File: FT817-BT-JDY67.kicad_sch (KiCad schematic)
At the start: 35 parts, among them J1009 Mini-DIN-8PR, J1010 Mini-DIN-6PR, Q1 2N7002, Q2 TP0610, U1 JDY-67 Bluetooth Module, U2 LM1117MP-5.0

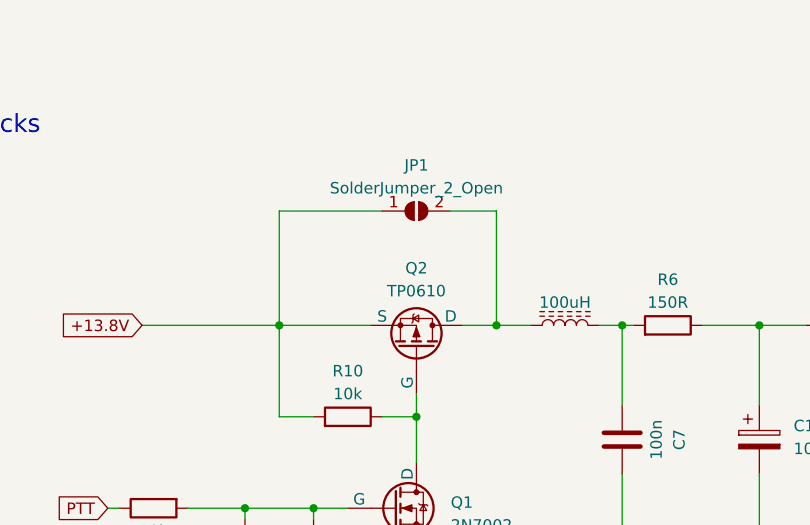
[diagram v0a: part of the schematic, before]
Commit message: Remove VCC control bypass jumper
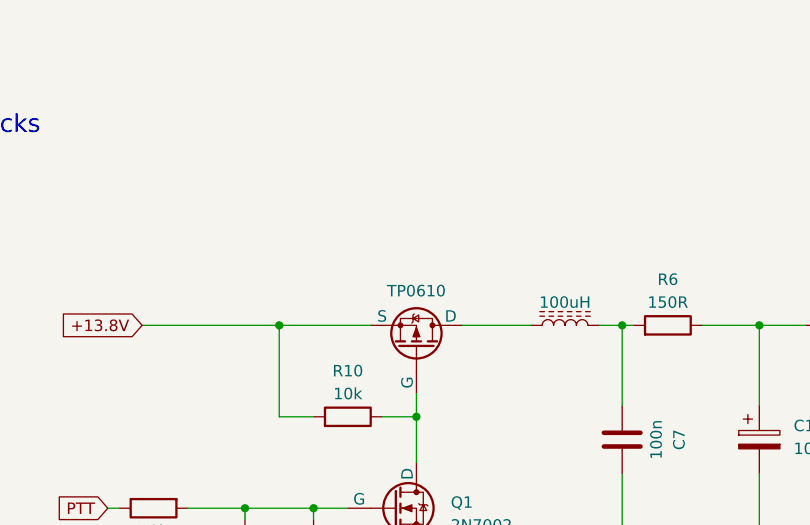
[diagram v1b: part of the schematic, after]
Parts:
- removed JP1: SolderJumper_2_Open, Jumper:SolderJumper-2_P1.3mm_Open_RoundedPad1.0x1.5mm, symbol Jumper:SolderJumper_2_Open
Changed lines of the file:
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@@
   (junction (at 204.47 144.78) (diameter 0) (color 0 0 0 0)
   )
-  (junction (at 171.45 50.8) (diameter 0) (color 0 0 0 0)
-  )
   (junction (at 147.32 50.8) (diameter 0) (color 0 0 0 0)
   )
@@
     (stroke (width 0) (type default))
   )
-  (wire (pts (xy 147.32 38.1) (xy 147.32 50.8))
-    (stroke (width 0) (type default))
-  )
   (wire (pts (xy 186.69 124.46) (xy 186.69 121.92))
     (stroke (width 0) (type default))
@@
     (stroke (width 0) (type default))
   )
-  (wire (pts (xy 167.64 50.8) (xy 171.45 50.8))
+  (wire (pts (xy 167.64 50.8) (xy 175.26 50.8))
     (stroke (width 0) (type default))
   )
@@
     (stroke (width 0) (type default))
   )
-  (wire (pts (xy 166.37 38.1) (xy 171.45 38.1))
-    (stroke (width 0) (type default))
-  )
   (wire (pts (xy 204.47 144.78) (xy 204.47 149.86))
     (stroke (width 0) (type default))
@@
     (stroke (width 0) (type default))
   )
-  (wire (pts (xy 171.45 38.1) (xy 171.45 50.8))
-    (stroke (width 0) (type default))
-  )
   (wire (pts (xy 137.16 71.12) (xy 143.51 71.12))
     (stroke (width 0) (type default))
@@
     (stroke (width 0) (type default))
   )
-  (wire (pts (xy 171.45 50.8) (xy 175.26 50.8))
-    (stroke (width 0) (type default))
-  )
   (wire (pts (xy 146.05 142.24) (xy 146.05 147.32))
-    (stroke (width 0) (type default))
-  )
-  (wire (pts (xy 158.75 38.1) (xy 147.32 38.1))
     (stroke (width 0) (type default))
   )
@@
     (in_bom yes) (on_board yes) (dnp no)
     (property "Reference" "Q2" (at 162.56 44.45 90)
-      (effects (font (size 1.27 1.27)))
+      (effects (font (size 1.27 1.27)) hide)
     )
     (property "Value" "TP0610" (at 162.56 46.99 90)
@@
         )
       )
-    )
-  )
-  (symbol (lib_id "Jumper:SolderJumper_2_Open") (at 162.56 38.1 0) (unit 1)
-    (in_bom yes) (on_board yes) (dnp no) (fields_autoplaced)
-    (property "Reference" "JP1" (at 162.56 33.02 0)
-      (effects (font (size 1.27 1.27)))
-    )
-    (property "Value" "SolderJumper_2_Open" (at 162.56 35.56 0)
-      (effects (font (size 1.27 1.27)))
-    )
-    (property "Footprint" "Jumper:SolderJumper-2_P1.3mm_Open_RoundedPad1.0x1.5mm" (at 162.56 38.1 0)
-      (effects (font (size 1.27 1.27)) hide)
-    )
-    (property "Datasheet" "~" (at 162.56 38.1 0)
-      (effects (font (size 1.27 1.27)) hide)
-    )
-    (pin "1")
-    (pin "2")
-    (instances
-      (project "FT817-BT-JDY67"
-        (path "/cfc49cd5-e50c-4df9-89f0-cc0db7d3dd1c"
-          (reference "JP1") (unit 1)
-        )
-      )

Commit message: update
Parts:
- Q1: symbol Simulation_SPICE:NMOS -> FT81x-BT_DIGI-Adapter_Library:NMOS
- Q2: symbol Simulation_SPICE:PMOS -> FT81x-BT_DIGI-Adapter_Library:PMOS
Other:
- note added: "Power Supplies"
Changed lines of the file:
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@@
   (title_block
     (title "FT-81x BT DIGI Adaptor")
-    (date "2023-05-27")
-    (rev "20230527")
+    (date "2023-06-08")
+    (rev "20230608")
     (company "https://github.com/BG6LH/FT-81x-BT-DIGI-Adaptor")
     (comment 1 "CC-BY-NC-SA 4.0")
@@
   (text "* Note\nMini-Din-6PR and Mini-Din-8PR are Standard Mini-Din Pins\nTo be mounted on back side of PCB.\nSo the footprints on front side are as same as FT-817's Mini-Din Jacks\nPTT pin here function as PS_ON control, don't pull low externally."
     (at 25.4 33.02 0)
+    (effects (font (size 2 2)) (justify left bottom))
+  )
+  (text "Power Supplies" (at 129.54 45.72 0)
     (effects (font (size 2 2)) (justify left bottom))
   )
@@
     )
   )
-  (symbol (lib_id "Simulation_SPICE:PMOS") (at 162.56 53.34 270) (mirror x) (unit 1)
+  (symbol (lib_id "FT81x-BT_DIGI-Adapter_Library:PMOS") (at 162.56 53.34 270) (mirror x) (unit 1)
     (in_bom yes) (on_board yes) (dnp no)
     (property "Reference" "Q2" (at 162.56 44.45 90)
-      (effects (font (size 1.27 1.27)) hide)
+      (effects (font (size 1.27 1.27)))
     )
     (property "Value" "TP0610" (at 162.56 46.99 90)
@@
     )
   )
-  (symbol (lib_id "Simulation_SPICE:NMOS") (at 160.02 71.12 0) (unit 1)
+  (symbol (lib_id "FT81x-BT_DIGI-Adapter_Library:NMOS") (at 160.02 71.12 0) (unit 1)
     (in_bom yes) (on_board yes) (dnp no) (fields_autoplaced)
     (property "Reference" "Q1" (at 166.37 70.485 0)

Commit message: Important update
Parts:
- removed Q1: 2N7002, Package_TO_SOT_SMD:SOT-23-3, symbol FT81x-BT_DIGI-Adapter_Library:NMOS
- removed Q2: TP0610, Package_TO_SOT_SMD:SOT-23-3, symbol FT81x-BT_DIGI-Adapter_Library:PMOS
- added Q1: 2N7002, Package_TO_SOT_SMD:SOT-23, symbol Library:2N7002
- added Q2: TP0610T, Package_TO_SOT_SMD:SOT-23, symbol Library:TP0610T
- C1, C2: symbol FT81x-BT_DIGI-Adapter_Library:C_Polarized -> Library:C_Polarized
- C3, C4, C5, C6, C7, C8: symbol FT81x-BT_DIGI-Adapter_Library:C -> Library:C
- D1, D2: symbol FT81x-BT_DIGI-Adapter_Library:LED -> Library:LED
- H1, H2: symbol FT81x-BT_DIGI-Adapter_Library:MountingHole_Pad -> Library:MountingHole_Pad
- H3: footprint FT81x-BT-DIGI-Adapter-Library:FT-817_GND_terminal_8.4mm_M8_Pad_TopBottom -> Library:FT-817_GND_terminal_8.4mm_M8_Pad_TopBottom; symbol FT81x-BT_DIGI-Adapter_Library:MountingHole_Pad -> Library:MountingHole_Pad
- J1009: footprint FT81x-BT-DIGI-Adapter-Library:MD-8Pin_Reverse -> Library:MD-8Pin_Reverse; symbol FT81x-BT_DIGI-Adapter_Library:Mini-DIN-8PR -> Library:Mini-DIN-8PR
- J1010: footprint FT81x-BT-DIGI-Adapter-Library:MD-6Pin_Reverse -> Library:MD-6Pin_Reverse; symbol FT81x-BT_DIGI-Adapter_Library:Mini-DIN-6PR -> Library:Mini-DIN-6PR
- L1, L2, L3: symbol FT81x-BT_DIGI-Adapter_Library:L_Ferrite -> Library:L_Ferrite
- R1, R10, R11, R12, R2, R3, R4, R5, R6, R7, R8, R9: symbol FT81x-BT_DIGI-Adapter_Library:R -> Library:R
- U1: footprint FT81x-BT-DIGI-Adapter-Library:JDY-67_Bluetooth_Module -> Library:JDY-67_Bluetooth_Module; symbol FT81x-BT_DIGI-Adapter_Library:JDY-67_Bluetooth_Module -> Library:JDY-67_Bluetooth_Module
- U2: symbol FT81x-BT_DIGI-Adapter_Library:LM1117MP-3.3 -> Library:LM1117MP-3.3
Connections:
- net +13.8V: now also Q2.2 (S)
- net GND: now also Q1.2 (S)
- net at C8.1, R11.1, R12.2: now also Q1.1 (G)
- net at R10.1: now also Q1.3 (D), Q2.1 (G)
- net at L3.1: now also Q2.3 (D)
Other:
- note added: "D"
- note added: "G"
- note added: "S"

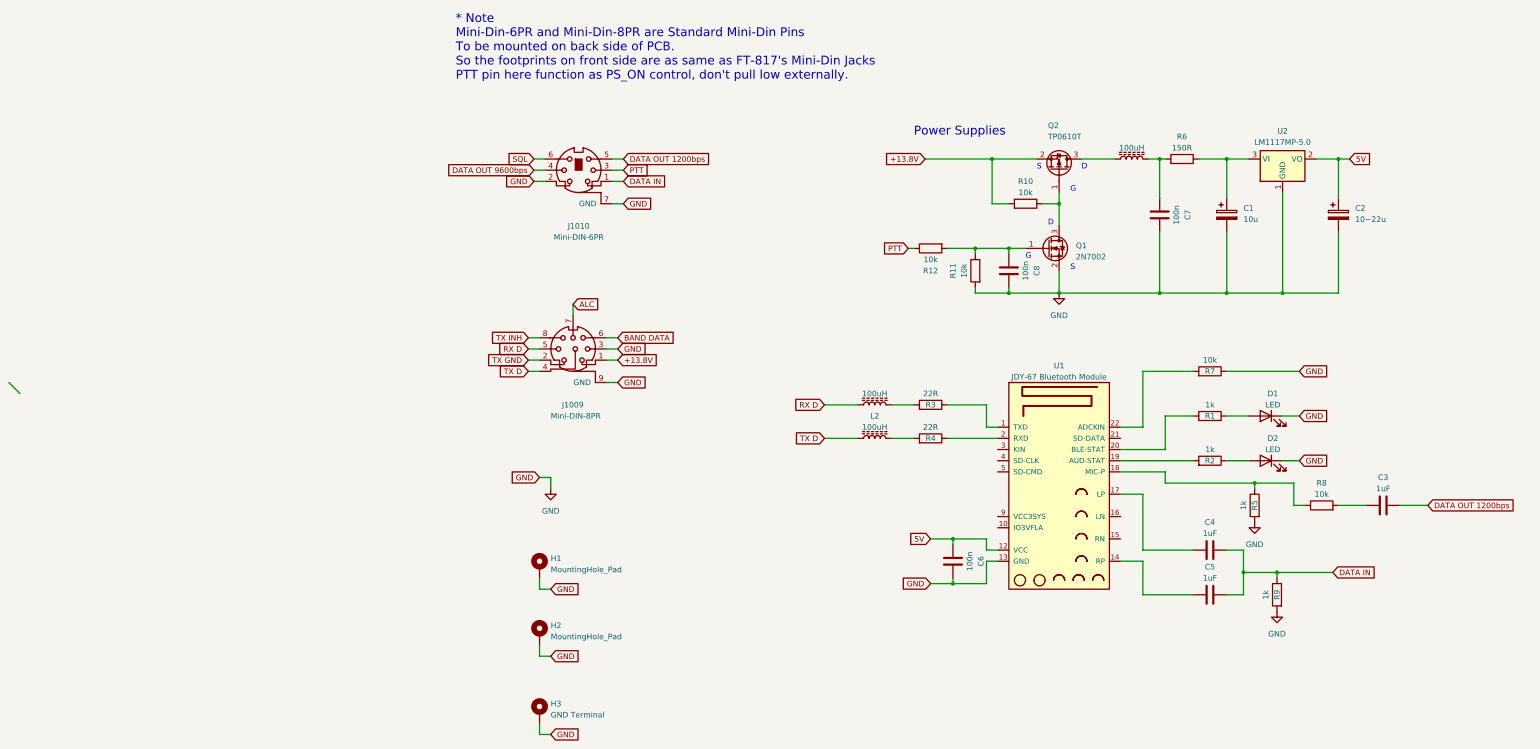
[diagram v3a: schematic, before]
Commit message: resistors value update
updated power supply's resistor right value.
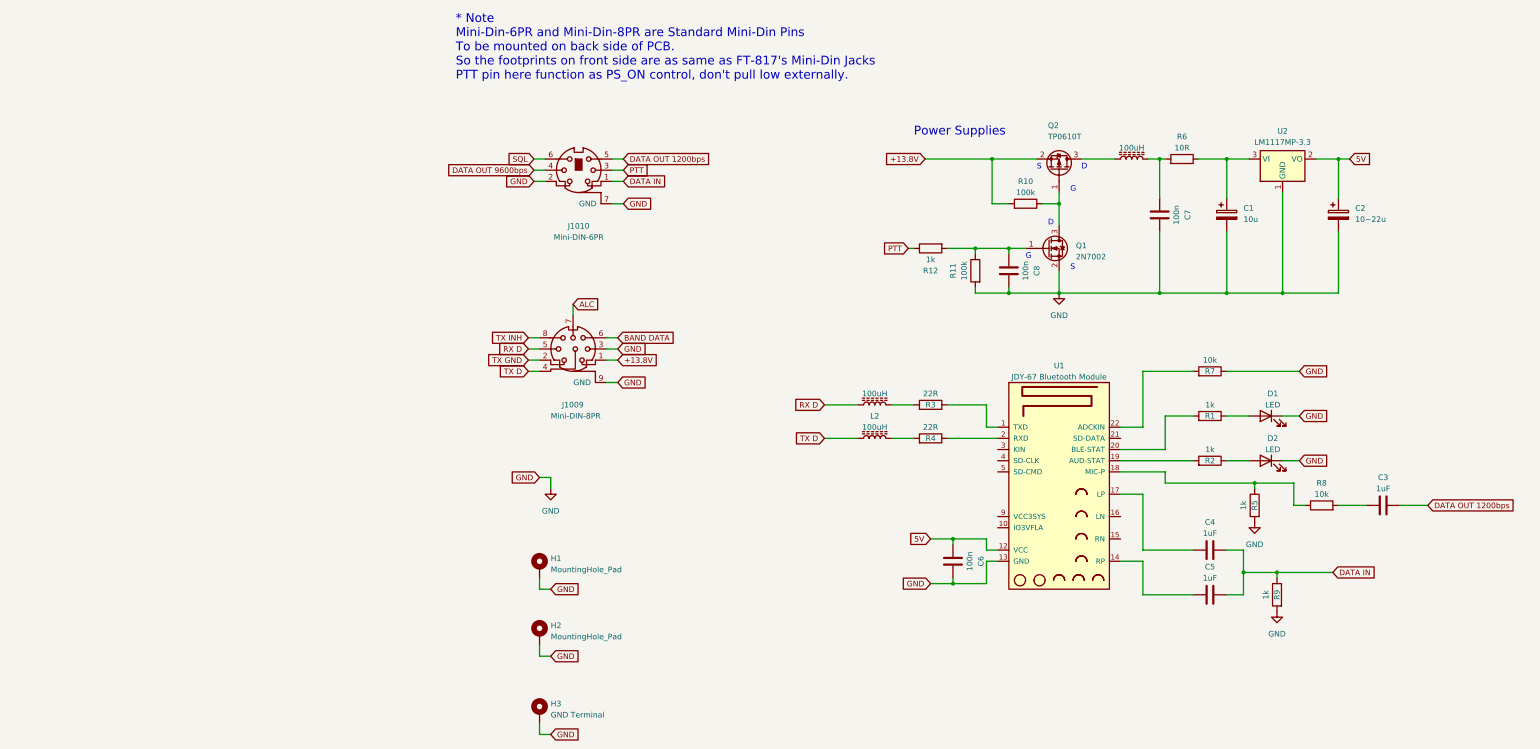
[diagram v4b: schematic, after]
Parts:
- R10, R11: value 10k -> 100k
- R12: value 10k -> 1k
- R6: value 150R -> 10R
- U2: value LM1117MP-5.0 -> LM1117MP-3.3
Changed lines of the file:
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@@
   (title_block
     (title "FT-81x BT DIGI Adaptor")
-    (date "2023-06-09")
+    (date "2024-01-20")
     (rev "20230609")
     (company "https://github.com/BG6LH/FT-81x-BT-DIGI-Adaptor")
@@
   (junction (at 200.66 81.28) (diameter 0) (color 0 0 0 0)
   )
-  (bus_entry (at -76.2 101.6) (size 2.54 2.54)
-    (stroke (width 0) (type default))
-  )
   (wire (pts (xy 138.43 137.16) (xy 146.05 137.16))
     (stroke (width 0) (type default))
@@
       (effects (font (size 1.27 1.27)))
     )
-    (property "Value" "10k" (at 140.97 76.2 90)
+    (property "Value" "100k" (at 140.97 76.2 90)
       (effects (font (size 1.27 1.27)))
     )
@@
       (effects (font (size 1.27 1.27)))
     )
-    (property "Value" "10k" (at 133.35 73.66 90)
+    (property "Value" "1k" (at 133.35 73.66 90)
       (effects (font (size 1.27 1.27)))
     )
@@
       (effects (font (size 1.27 1.27)))
     )
-    (property "Value" "10k" (at 154.94 58.42 90)
+    (property "Value" "100k" (at 154.94 58.42 90)
       (effects (font (size 1.27 1.27)))
     )
@@
       (effects (font (size 1.27 1.27)))
     )
-    (property "Value" "LM1117MP-5.0" (at 213.36 46.99 0)
+    (property "Value" "LM1117MP-3.3" (at 213.36 46.99 0)
       (effects (font (size 1.27 1.27)))
     )
@@
       (effects (font (size 1.27 1.27)))
     )
-    (property "Value" "150R" (at 190.5 48.26 90)
-      (effects (font (size 1.27 1.27)))
-    )
+    (property "Value" "10R" (at 190.5 48.26 90)
+      (effects (font (size 1.27 1.27)))
+    )
